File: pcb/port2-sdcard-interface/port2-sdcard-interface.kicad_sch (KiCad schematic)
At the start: 55 parts, among them J2 P2000T Port 2, J3 SD Card, U1 CY62128ELL-45SXI, U10 74HC32, U11 74HC273, U12 74HC165, U13 74HC595, U14 74HC00, U15 SST39SF010, U17 74HC138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

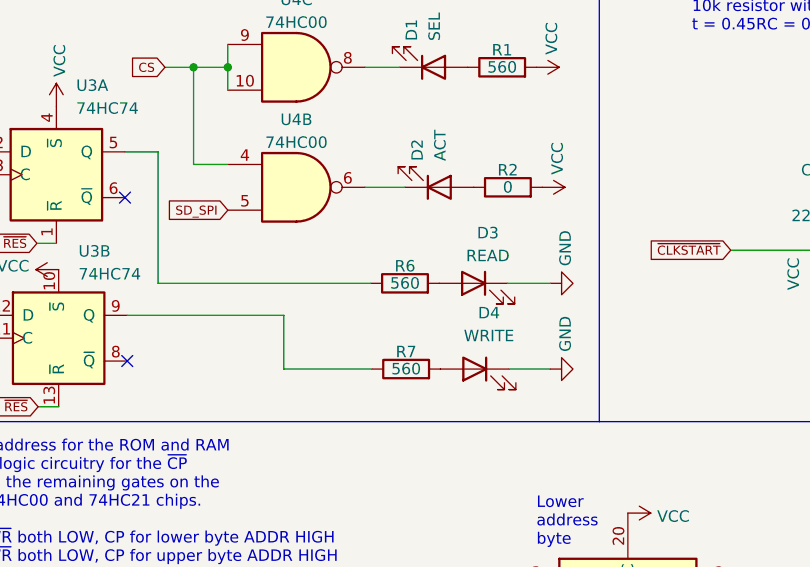
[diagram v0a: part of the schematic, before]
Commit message: Changing resistor value
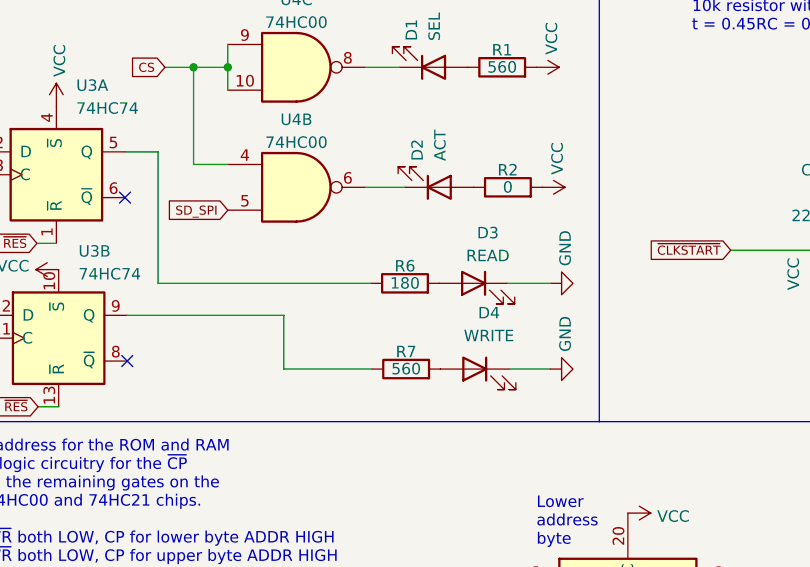
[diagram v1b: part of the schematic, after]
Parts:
- R6: value 560 -> 180
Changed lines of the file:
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@@
       (effects (font (size 1.27 1.27)))
     )
-    (property "Value" "560" (at 231.14 155.448 90)
+    (property "Value" "180" (at 231.14 155.448 90)
       (effects (font (size 1.27 1.27)))
     )

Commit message: PCB revision 6 (#9)
* Setting port addresses in header and include files

* Updating rev and changing 0x60 to 0x40

* Changing port for BASICmod

* Incrementing version number

* Adding enclosure files, changing CI and adding option to disable hardware test

* Fixing CI

* Adding README.md
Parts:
- removed J3: SD Card, Connector_PinSocket_2.54mm:PinSocket_1x06_P2.54mm_Vertical, symbol Connector:Conn_01x06_Socket
- added C23: 100nF, Capacitor_SMD:C_1206_3216Metric_Pad1.33x1.80mm_HandSolder, symbol Device:C
- added J1: Micro_SD_Card_Det1, components:CONN9_MSD-1_CUD, symbol Connector:Micro_SD_Card_Det1
- added R10, R11, R8, R9: 3.3k, Resistor_SMD:R_0805_2012Metric_Pad1.20x1.40mm_HandSolder, symbol Device:R
- added U16: AMS1117-3.3, Package_TO_SOT_SMD:SOT-223-3_TabPin2, symbol Regulator_Linear:AMS1117-3.3
- added U21: 74LVC125, Package_SO:TSSOP-14_4.4x5mm_P0.65mm, symbol 74xx:74LVC125
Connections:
- net CLK: now also R10.1
- net GND: now also U20.12 (A1), C23.2, J1.6 (VSS), U16.1 (GND), U21.1, U21.10, U21.13, U21.4, U21.7 (GND)
- net MISO: now also U21.11
- net MOSI: now also R9.1
- net VCC: now also U16.3 (VI); no longer U20.12 (A1)
- net ~{CS}: now also R11.1
- new net: R11.2, U21.9
- new net: R10.2, U21.5
- new net: R8.2, U21.12
- new net: R9.2, U21.2
- new net +3V3: C23.1, J1.4 (VDD), U16.2 (VO), U21.14 (VCC)
- new net CS_LLS: J1.2 (DAT3/CD), U21.8
- new net D0_LLS: J1.7 (DAT0), R8.1
- new net DI_LLS: J1.3 (CMD), U21.3
- new net SCK_LLS: J1.5 (CLK), U21.6
- no-connect marks 24 -> 28
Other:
- note added: "$48: ADDR LOW $49: ADDR HIGH $4A: BANK ROM $4B: BANK RAM $4C: ROM $4D: RAM"
- note added: "Note: 74LVC125 needs 3v3 on VCC"
- note added: "in $40: ~{SER_RD} is pulled low, reading from the in register. in $41: Does nothing in $42: ~{SDOUT_SET} is pulled low, pulling MISO low via a 10k resistor. in $43: ~{SDOUT_RESET} is pulled low, pulling MISO high via a 10k resistor. When no card is present, the output of the SD card will follow the output of the SET/RESET latch, however if a card is present, though unresponsive, it will not follo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"
- note added: "out $40: ~{SER_WR} is pulled low, loading the values on the data bus into the out register. out $41: ~{CLKSTART} is pulled low, starting the counter circuit and pushing a byte into the SD card while simultaneously reading a byte. out $42: ~{SDCS_SET} is pulled low, pulling ~{CS} high, deactivating the SD card. out $43: ~{SDCS_RESET} is pulled low, pulling ~{CS} low, activating the SD card."
- note removed: "$68: ADDR LOW $69: ADDR HIGH $6A: BANK ROM $6B: BANK RAM $6C: ROM $6D: RAM"
- note removed: "in $60: ~{SER_RD} is pulled low, reading from the in register. in $61: Does nothing in $62: ~{SDOUT_SET} is pulled low, pulling MISO low via a 10k resistor. in $63: ~{SDOUT_RESET} is pulled low, pulling MISO high via a 10k resistor. When no card is present, the output of the SD card will follow the output of the SET/RESET latch, however if a card is present, though unresponsive, it will not follo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"
- note removed: "out $60: ~{SER_WR} is pulled low, loading the values on the data bus into the out register. out $61: ~{CLKSTART} is pulled low, starting the counter circuit and pushing a byte into the SD card while simultaneously reading a byte. out $62: ~{SDCS_SET} is pulled low, pulling ~{CS} high, deactivating the SD card. out $63: ~{SDCS_RESET} is pulled low, pulling ~{CS} low, activating the SD card."
- moved on the sheet: J2, U19E, U20, U7C

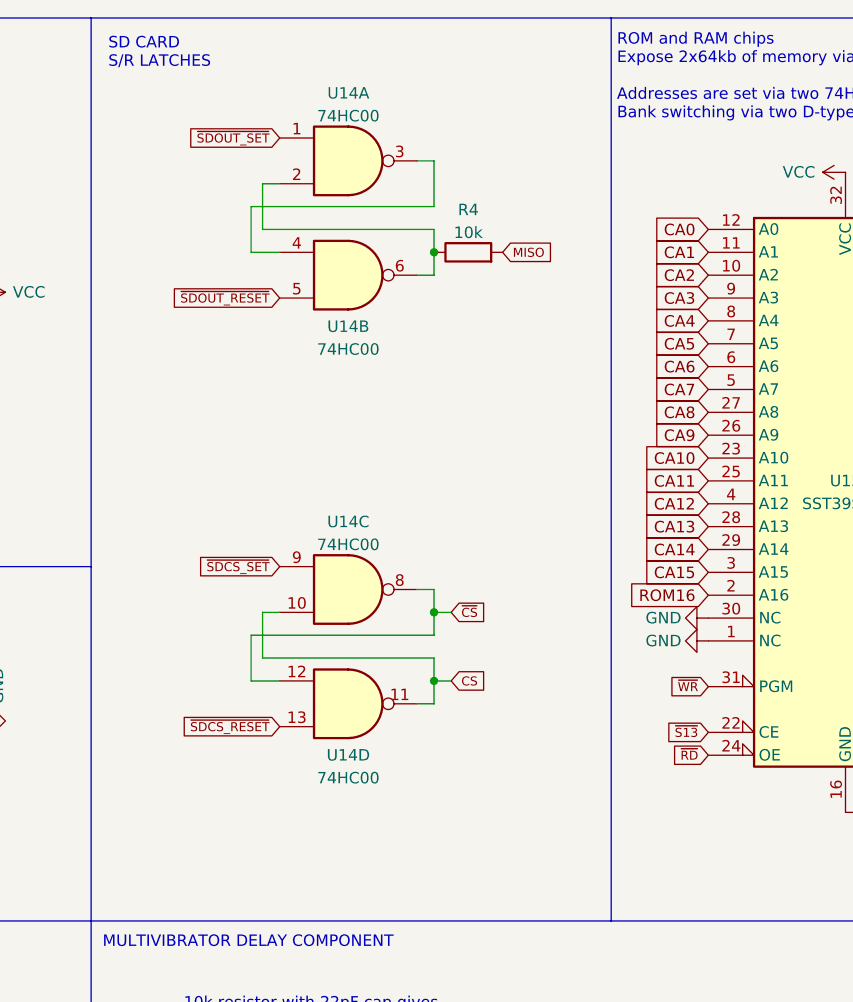
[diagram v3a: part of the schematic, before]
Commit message: Creating separate SD-CARD test cartridge and modifying SD-card detection routine
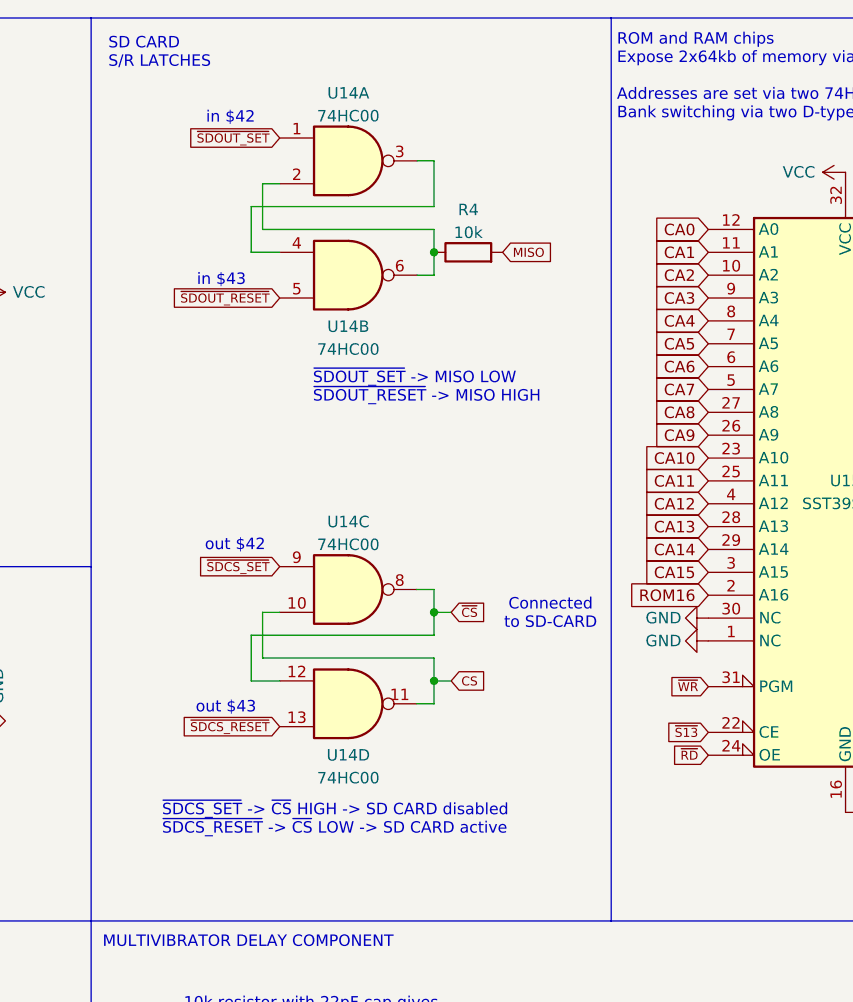
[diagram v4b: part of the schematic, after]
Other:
- note added: "Connected to SD-CARD"
- note added: "in $42"
- note added: "in $43"
- note added: "out $42"
- note added: "out $43"
- note added: "~{SDCS_SET} -> ~{CS} HIGH -> SD CARD disabled ~{SDCS_RESET} -> ~{CS} LOW -> SD CARD active"
- note added: "~{SDOUT_SET} -> MISO LOW ~{SDOUT_RESET} -> MISO HIGH"
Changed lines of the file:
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@@
+		)
+	)
+	(text "in $42"
+		(exclude_from_sim no)
+		(at 268.224 26.416 0)
+		(effects
+			(font
+				(size 1.27 1.27)
+			)
 		)
 	)
@@
 		)
 	)
+	(text "Connected \nto SD-CARD"
+		(exclude_from_sim no)
+		(at 303.784 81.534 0)
+		(effects
+			(font
+				(size 1.27 1.27)
+			)
+		)
+	)
 	(text "SD CARD"
 		(exclude_from_sim no)
@@
 		)
 	)
+	(text "~{SDOUT_SET} -> MISO LOW\n~{SDOUT_RESET} -> MISO HIGH"
+		(exclude_from_sim no)
+		(at 277.368 56.388 0)
+		(effects
+			(font
+				(size 1.27 1.27)
+			)
+			(justify left)
+		)
+	)
+	(text "~{SDCS_SET} -> ~{CS} HIGH -> SD CARD disabled\n~{SDCS_RESET} -> ~{CS} LOW -> SD CARD active"
+		(exclude_from_sim no)
+		(at 260.604 104.394 0)
+		(effects
+			(font
+				(size 1.27 1.27)
+			)
+			(justify left)
+		)
+	)
 	(text "SELECTION COMPONENT"
 		(exclude_from_sim no)
@@
 		)
 	)
+	(text "in $43"
+		(exclude_from_sim no)
+		(at 267.208 44.45 0)
+		(effects
+			(font
+				(size 1.27 1.27)
+			)
+		)
+	)
 	(text "Both CEP and CET need\nto be high for count\nto be enabled."
 		(exclude_from_sim no)
@@
 		)
 	)
+	(text "out $42"
+		(exclude_from_sim no)
+		(at 268.732 73.914 0)
+		(effects
+			(font
+				(size 1.27 1.27)
+			)
+		)
+	)
+	(text "out $43"
+		(exclude_from_sim no)
+		(at 267.716 91.948 0)
+		(effects
+			(font
+				(size 1.27 1.27)
+			)
+		)
+	)

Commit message: Version 0.8.0 (#13)
* Initial commit diagnostics cartridge and fixing bug allowing for more diverse sd-cards.

* Removing map file

* Fix bug in reporting partition capactities

* Finding file and folders in diag cartridge

* Polishing output

* Storing writetest

* Moving folder

* Adding explanation to test

* Creating BOM/CPL for assembly service

* ReOptimizing instructions

* End of day commit

* Timeout and data errors

* Succesfully creating new file

* Polishing FAT32 routines

* Further polishing code

* Adding file pointer creation

* Writing to file

* Writing data to SD card

* Initial commit cassette dump cartridge

* Dumping cassette to SD-card

* Further polishing code for cassette dump

* Refactoring repo

* Polishing cassette dump utility

* Fixing bug reading invalid folder

* Adding casdump to GA

* Expanding README.md

* Adding csv files

* Adjusting image
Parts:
- C1, C10, C11, C12, C13, C14, C15, C16, C17, C18, C19, C2, C22, C3, C4, C5, C6, C7, C8, C9: LCSC Part C126469 -> (none); LCSC Part # (none) -> C126469
- C20, C21: LCSC Part C525286 -> (none); LCSC Part # (none) -> C525286
- C23: LCSC Part # (none) -> C309030
- J1: LCSC Part # (none) -> C381082
- R1, R6, R7: LCSC Part C429158 -> (none); LCSC Part # (none) -> C429158
- R10, R11, R8, R9: LCSC Part # (none) -> C407459
- R2: LCSC Part # (none) -> C431818
- R3, R4: LCSC Part C5159708 -> (none); LCSC Part # (none) -> C5159708
- R5: LCSC Part C5123594 -> (none); LCSC Part # (none) -> C5123594
- U1: LCSC Part C2840304 -> (none); LCSC Part # (none) -> C2840304
- U10, U9: LCSC Part C5632 -> (none); LCSC Part # (none) -> C5632
- U11, U8: LCSC Part C131486 -> (none); LCSC Part # (none) -> C131486
- U12: LCSC Part C5613 -> (none); LCSC Part # (none) -> C5613
- U13: LCSC Part C5947 -> (none); LCSC Part # (none) -> C5947
- U14, U2, U4: LCSC Part C699445 -> (none); LCSC Part # (none) -> C699445
- U16: LCSC Part # (none) -> C5346136
- U17, U6: LCSC Part C5602 -> (none); LCSC Part # (none) -> C5602
- U18, U3: LCSC Part C27597 -> (none); LCSC Part # (none) -> C27597
- U19: LCSC Part C5588 -> (none); LCSC Part # (none) -> C5588
- U20: LCSC Part C5953 -> (none); LCSC Part # (none) -> C5953
- U21: LCSC Part # (none) -> C7494906
- U5: LCSC Part C338758 -> (none); LCSC Part # (none) -> C338758
- U7: LCSC Part C5597 -> (none); LCSC Part # (none) -> C5597

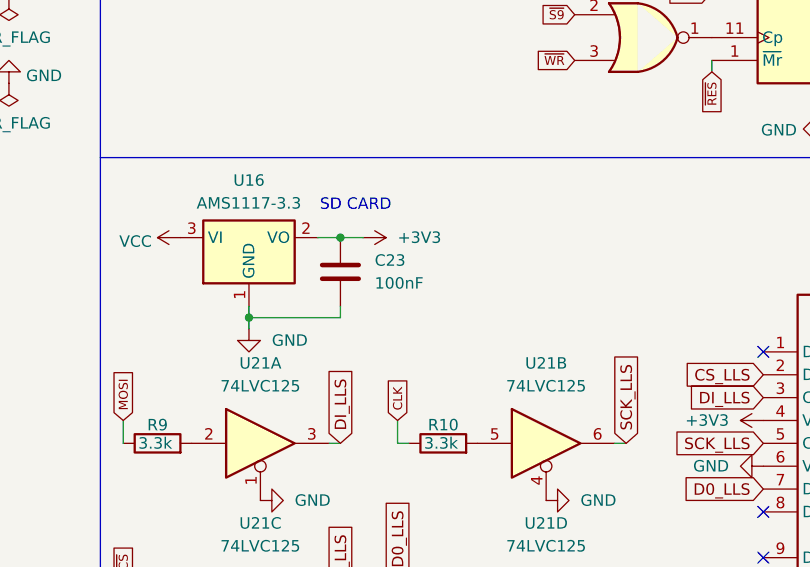
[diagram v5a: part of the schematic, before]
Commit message: Fixing value in schematic
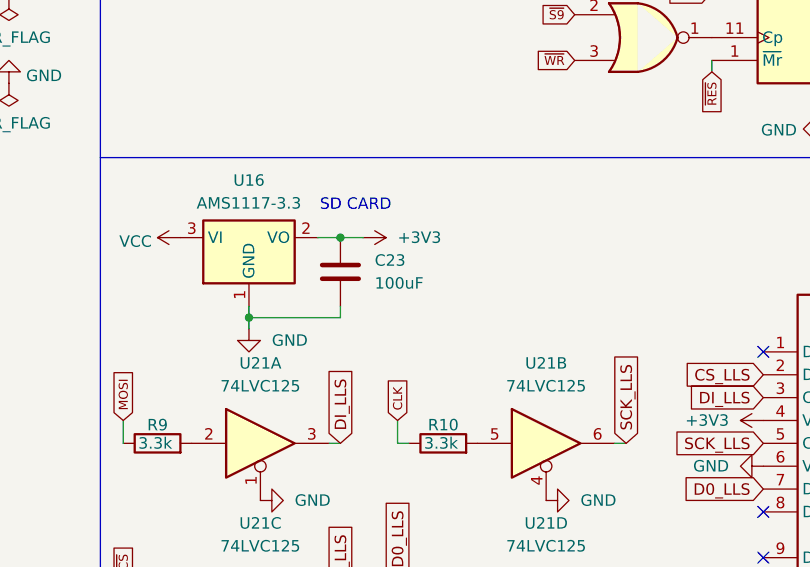
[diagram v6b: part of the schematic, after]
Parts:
- C23: value 100nF -> 100uF
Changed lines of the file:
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@@
 			)
 		)
-		(property "Value" "100nF"
+		(property "Value" "100uF"
 			(at 205.74 238.7599 0)
 			(effects
